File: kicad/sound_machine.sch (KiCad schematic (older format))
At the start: 18 parts, among them J1 Conn_01x04, J10 Conn_01x01, J11 Conn_01x01, J12 Conn_01x01, J13 Conn_01x15, J16 Conn_01x15, J2 Conn_01x15, J3 Conn_01x15, J4 Conn_01x08, J5 Audio-Jack-3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

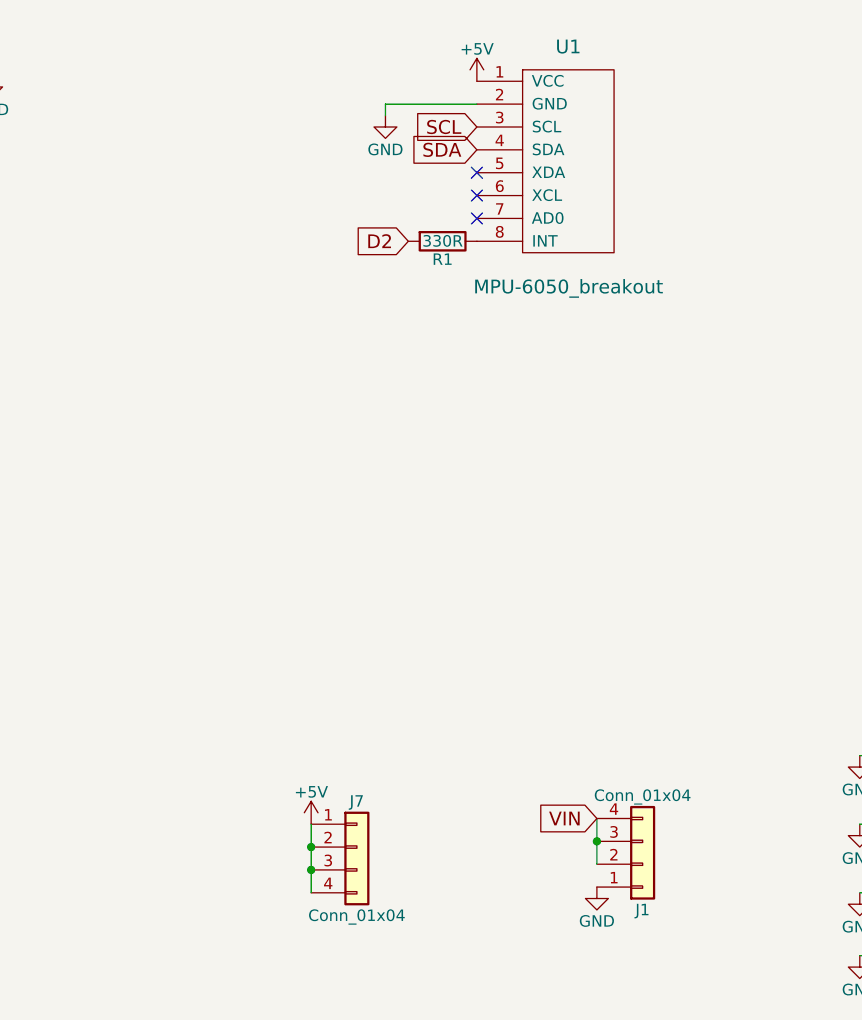
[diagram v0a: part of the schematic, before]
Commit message: Logos & labels
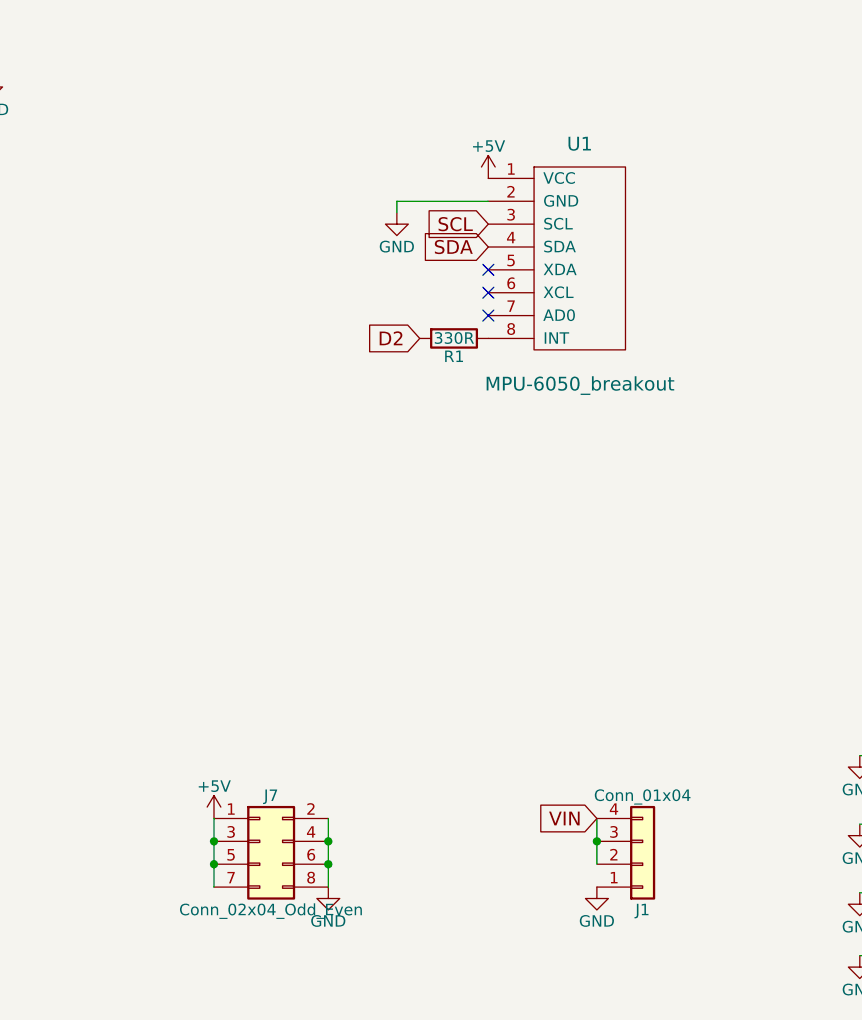
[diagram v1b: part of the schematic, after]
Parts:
- removed J7: Conn_01x04, Pin_Headers:Pin_Header_Straight_1x04_Pitch2.54mm, symbol Conn_01x04
- added J7: Conn_02x04_Odd_Even, Pin_Headers:Pin_Header_Straight_2x04_Pitch2.54mm, symbol Conn_02x04_Odd_Even
- J10, J11, J12, J9: footprint Mounting_Holes:MountingHole_3.2mm_M3_Pad -> Mounting_Holes:MountingHole_3.2mm_M3_DIN965_Pad
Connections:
- net +5V: now also J7.1 (Pin_1), J7.3 (Pin_3), J7.5 (Pin_5), J7.7 (Pin_7)
- net GND: now also J7.2 (Pin_2), J7.4 (Pin_4), J7.6 (Pin_6), J7.8 (Pin_8)
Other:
- moved on the sheet: R1, U1
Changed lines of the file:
@@
 L MPU-6050_breakout U1
 U 1 1 59A0448B
-P 8850 2125
-F 0 "U1" H 8850 2625 60  0000 C CNN
-F 1 "MPU-6050_breakout" H 8850 1575 60  0000 C CNN
-F 2 "sound_machine:MPU-6050" H 8350 2125 60  0001 C CNN
-F 3 "" H 8350 2125 60  0001 C CNN
-	1    8850 2125
+P 8900 2550
+F 0 "U1" H 8900 3050 60  0000 C CNN
+F 1 "MPU-6050_breakout" H 8900 2000 60  0000 C CNN
+F 2 "sound_machine:MPU-6050" H 8400 2550 60  0001 C CNN
+F 3 "" H 8400 2550 60  0001 C CNN
+	1    8900 2550
 	1    0    0    -1
 $EndComp
@@
 	1    0    0    -1
 $EndComp
-Text GLabel 8450 2075 0    60   Input ~ 0
+Text GLabel 8500 2500 0    60   Input ~ 0
 SDA
-Text GLabel 8450 1975 0    60   Input ~ 0
+Text GLabel 8500 2400 0    60   Input ~ 0
 SCL
 $Comp
 L GND #PWR04
 U 1 1 59A053B4
-P 8050 1925
-F 0 "#PWR04" H 8050 1675 50  0001 C CNN
-F 1 "GND" H 8050 1775 50  0000 C CNN
-F 2 "" H 8050 1925 50  0001 C CNN
-F 3 "" H 8050 1925 50  0001 C CNN
-	1    8050 1925
-	1    0    0    -1
-$EndComp
-NoConn ~ 8450 2175
-NoConn ~ 8450 2275
+P 8100 2350
+F 0 "#PWR04" H 8100 2100 50  0001 C CNN
+F 1 "GND" H 8100 2200 50  0000 C CNN
+F 2 "" H 8100 2350 50  0001 C CNN
+F 3 "" H 8100 2350 50  0001 C CNN
+	1    8100 2350
+	1    0    0    -1
+$EndComp
+NoConn ~ 8500 2600
+NoConn ~ 8500 2700
 $Comp
 L +5V #PWR05
 U 1 1 5A3D7C1F
-P 8450 1775
-F 0 "#PWR05" H 8450 1625 50  0001 C CNN
-F 1 "+5V" H 8450 1915 50  0000 C CNN
-F 2 "" H 8450 1775 50  0001 C CNN
-F 3 "" H 8450 1775 50  0001 C CNN
-	1    8450 1775
+P 8500 2200
+F 0 "#PWR05" H 8500 2050 50  0001 C CNN
+F 1 "+5V" H 8500 2340 50  0000 C CNN
+F 2 "" H 8500 2200 50  0001 C CNN
+F 3 "" H 8500 2200 50  0001 C CNN
+	1    8500 2200
 	1    0    0    -1
 $EndComp
@@
 Text GLabel 4475 2350 2    60   Input ~ 0
 SDA
-Text GLabel 8150 2475 0    60   Input ~ 0
+Text GLabel 8200 2900 0    60   Input ~ 0
 D2
 $Comp
 L R R1
 U 1 1 5A3D88B7
-P 8300 2475
-F 0 "R1" V 8380 2475 50  0000 C CNN
-F 1 "330R" V 8300 2475 50  0000 C CNN
-F 2 "Resistors_SMD:R_0805_HandSoldering" V 8230 2475 50  0001 C CNN
-F 3 "" H 8300 2475 50  0001 C CNN
-	1    8300 2475
+P 8350 2900
+F 0 "R1" V 8430 2900 50  0000 C CNN
+F 1 "330R" V 8350 2900 50  0000 C CNN
+F 2 "Resistors_SMD:R_0805_HandSoldering" V 8280 2900 50  0001 C CNN
+F 3 "" H 8350 2900 50  0001 C CNN
+	1    8350 2900
 	0    1    1    0
 $EndComp
-NoConn ~ 8450 2375
+NoConn ~ 8500 2800
 $Comp
 L Audio-Jack-3 J5
@@
 F 0 "J9" H 10525 4825 50  0000 C CNN
 F 1 "Conn_01x01" H 10525 4625 50  0000 C CNN
-F 2 "Mounting_Holes:MountingHole_3.2mm_M3_Pad" H 10525 4725 50  0001 C CNN
+F 2 "Mounting_Holes:MountingHole_3.2mm_M3_DIN965_Pad" H 10525 4725 50  0001 C CNN
 F 3 "" H 10525 4725 50  0001 C CNN
 	1    10525 4725
@@
 F 0 "J10" H 10525 5125 50  0000 C CNN
 F 1 "Conn_01x01" H 10525 4925 50  0000 C CNN
-F 2 "Mounting_Holes:MountingHole_3.2mm_M3_Pad" H 10525 5025 50  0001 C CNN
+F 2 "Mounting_Holes:MountingHole_3.2mm_M3_DIN965_Pad" H 10525 5025 50  0001 C CNN
 F 3 "" H 10525 5025 50  0001 C CNN
 	1    10525 5025
@@
 F 0 "J11" H 10525 5425 50  0000 C CNN
 F 1 "Conn_01x01" H 10525 5225 50  0000 C CNN
-F 2 "Mounting_Holes:MountingHole_3.2mm_M3_Pad" H 10525 5325 50  0001 C CNN
+F 2 "Mounting_Holes:MountingHole_3.2mm_M3_DIN965_Pad" H 10525 5325 50  0001 C CNN
 F 3 "" H 10525 5325 50  0001 C CNN
 	1    10525 5325
@@
 F 0 "J12" H 10525 5700 50  0000 C CNN
 F 1 "Conn_01x01" H 10525 5500 50  0000 C CNN
-F 2 "Mounting_Holes:MountingHole_3.2mm_M3_Pad" H 10525 5600 50  0001 C CNN
+F 2 "Mounting_Holes:MountingHole_3.2mm_M3_DIN965_Pad" H 10525 5600 50  0001 C CNN
 F 3 "" H 10525 5600 50  0001 C CNN
 	1    10525 5600
@@
 	3250 4175 3250 4050
 Wire Wire Line
-	8450 1875 8050 1875
-Wire Wire Line
-	8050 1875 8050 1925
+	8500 2300 8100 2300
+Wire Wire Line
+	8100 2300 8100 2350
 Wire Wire Line
 	2075 1975 2425 1975
@@
 	3425 4375 3800 4375
 $Comp
-L Conn_01x04 J7
-U 1 1 5A3E45A3
-P 7925 5125
-F 0 "J7" H 7925 5325 50  0000 C CNN
-F 1 "Conn_01x04" H 7925 4825 50  0000 C CNN
-F 2 "Pin_Headers:Pin_Header_Straight_1x04_Pitch2.54mm" H 7925 5125 50  0001 C CNN
-F 3 "" H 7925 5125 50  0001 C CNN
-	1    7925 5125
-	1    0    0    -1
-$EndComp
-$Comp
 L +5V #PWR020
 U 1 1 5A3E468E
-P 7725 5025
-F 0 "#PWR020" H 7725 4875 50  0001 C CNN
-F 1 "+5V" H 7725 5165 50  0000 C CNN
-F 2 "" H 7725 5025 50  0001 C CNN
-F 3 "" H 7725 5025 50  0001 C CNN
-	1    7725 5025
-	1    0    0    -1
-$EndComp
-Wire Wire Line
-	7725 5025 7725 5325
-Connection ~ 7725 5125
-Connection ~ 7725 5225
+P 7300 5000
+F 0 "#PWR020" H 7300 4850 50  0001 C CNN
+F 1 "+5V" H 7300 5140 50  0000 C CNN
+F 2 "" H 7300 5000 50  0001 C CNN
+F 3 "" H 7300 5000 50  0001 C CNN
+	1    7300 5000
+	1    0    0    -1
+$EndComp
 $Comp
 L Conn_01x04 J1
@@
 	8975 5000 8975 5200
 Connection ~ 8975 5100
+$Comp
+L GND #PWR021
+U 1 1 5A3EB1D3
+P 7800 5300
+F 0 "#PWR021" H 7800 5050 50  0001 C CNN
+F 1 "GND" H 7800 5150 50  0000 C CNN
+F 2 "" H 7800 5300 50  0001 C CNN
+F 3 "" H 7800 5300 50  0001 C CNN
+	1    7800 5300
+	1    0    0    -1
+$EndComp
+Wire Wire Line
+	7300 5000 7300 5300
+Connection ~ 7300 5100
+Connection ~ 7300 5200
+Wire Wire Line
+	7800 5000 7800 5300
+Connection ~ 7800 5100
+Connection ~ 7800 5200
+$Comp
+L Conn_02x04_Odd_Even J7
+U 1 1 5A3EBA65
+P 7500 5100
+F 0 "J7" H 7550 5300 50  0000 C CNN
+F 1 "Conn_02x04_Odd_Even" H 7550 4800 50  0000 C CNN
+F 2 "Pin_Headers:Pin_Header_Straight_2x04_Pitch2.54mm" H 7500 5100 50  0001 C CNN
+F 3 "" H 7500 5100 50  0001 C CNN
+	1    7500 5100
+	1    0    0    -1
+$EndComp
 $EndSCHEMATC
